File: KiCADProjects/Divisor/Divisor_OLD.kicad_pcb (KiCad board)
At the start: 2 copper layers, 94.2 x 94.6 mm, 34 parts, among them J1 SMA_Female, J10 SMA_Female, J11 SMA_Female, J12 SMA_Female, J13 SMA_Female, J14 SMA_Female, J15 SMA_Female, J16 SMA_Female, J17 SMA_Female, J2 SMA_Female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

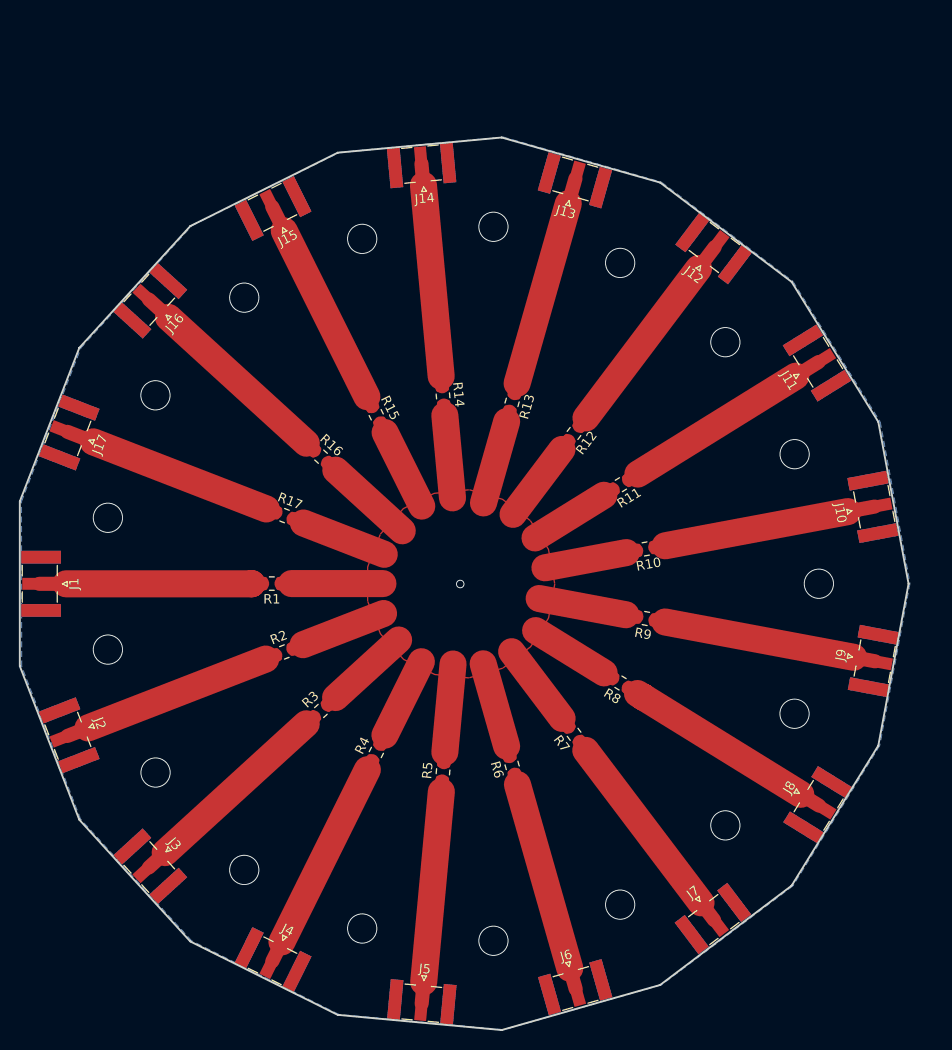
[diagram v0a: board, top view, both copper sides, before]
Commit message: Modificaciones varias al divisor
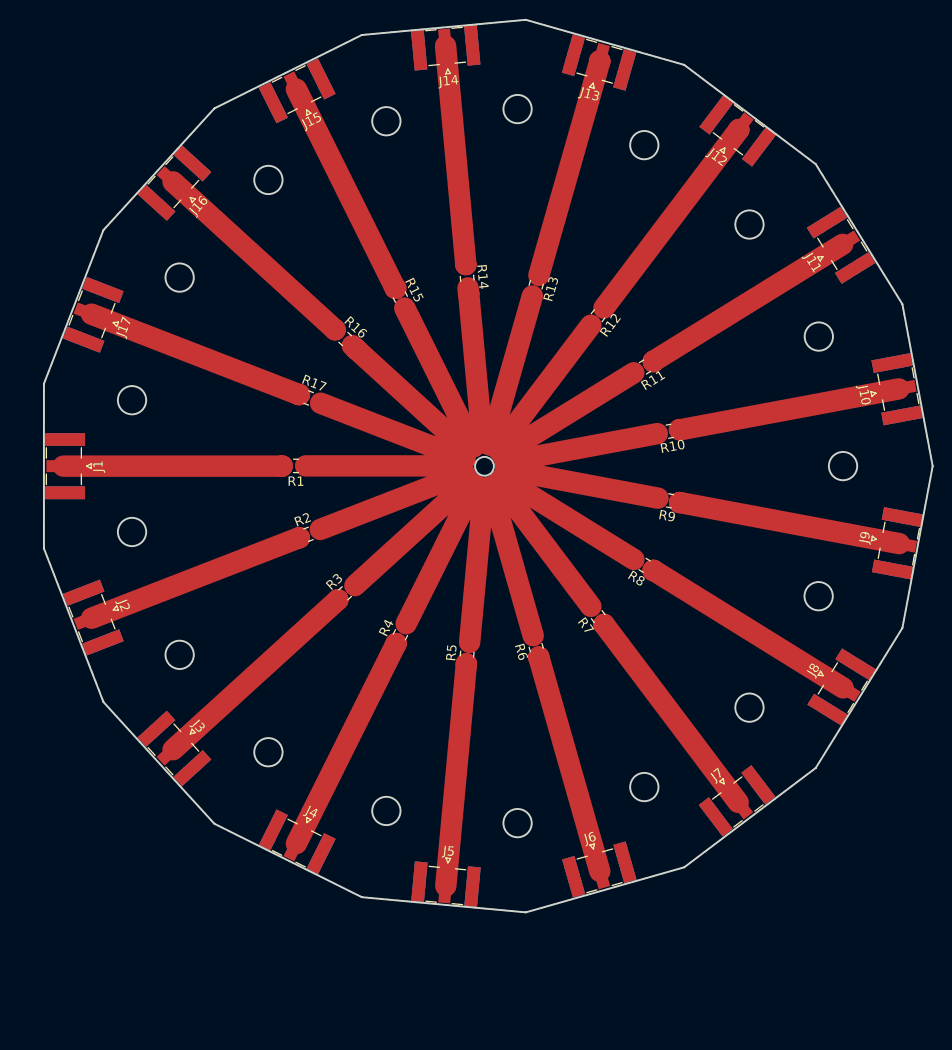
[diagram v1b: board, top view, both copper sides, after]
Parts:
- moved J14 12.7 mm to (129.6, 37.2)
- moved J16 12.7 mm to (100.8, 51.5)
- moved R4 12.7 mm to (124.8, 99.4)
- moved R11 12.7 mm to (150.7, 71.0)
- moved R14 12.7 mm to (131.9, 61.6)
- moved J12 12.7 mm to (160.5, 46.0)
- moved R16 12.7 mm to (118.9, 68.0)
- moved J5 12.7 mm to (129.6, 125.8)
- moved J15 12.7 mm to (113.8, 41.7)
- moved R17 12.7 mm to (115.1, 74.3)
- moved R12 12.7 mm to (145.7, 65.6)
- moved R8 12.7 mm to (150.7, 92.0)
- moved R10 12.7 mm to (153.3, 77.8)
- moved J10 12.7 mm to (177.4, 73.3)
- moved R5 12.7 mm to (131.9, 101.4)
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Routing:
- net Net-(R1-Pad1): track 171.3 -> 279.4 mm, vias 1 -> 0
- net GND: vias 17 -> 0
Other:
- outline, holes or cut-outs redrawn
- net class Default: clearance 0.5 -> 0.2; trace_width 2.87 -> 2.27
- rule trace_clearance: 0.5 -> 0.2
- board text removed: "DIVISOR DE POTENCIA 1 X 16 TELECO IB 2020 REV. M-1.0"
